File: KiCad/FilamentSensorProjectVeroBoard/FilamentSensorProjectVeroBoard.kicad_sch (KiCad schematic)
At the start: 7 parts, among them J1 Power input, J2 NeoPixels JST-PH, J3 Audio JST-PH, J4 Power JST-PH, J5 Power JST-PH, SW1 Power switch, U1 MCU ESP32-C3 Mini

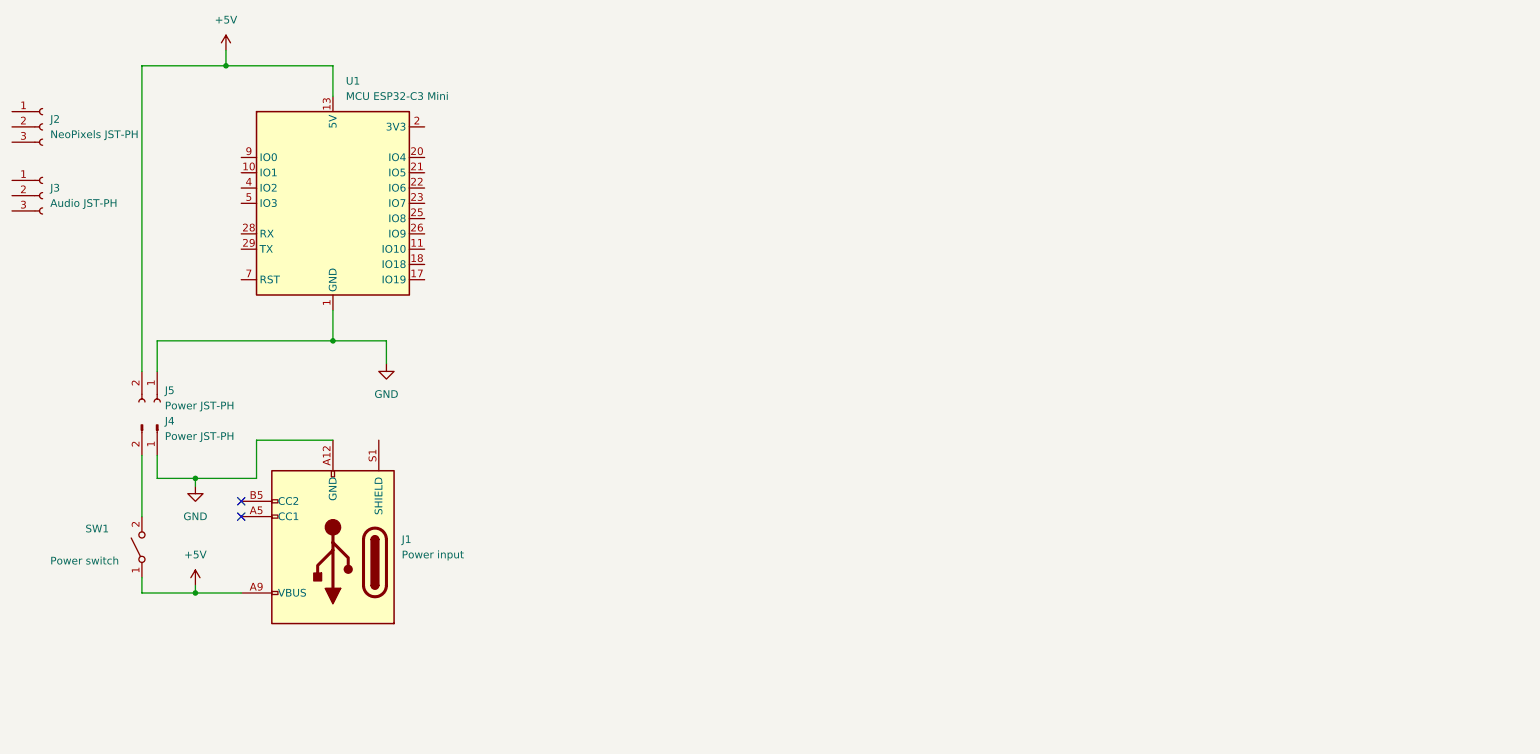
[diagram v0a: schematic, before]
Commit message: Added Vero Board Shematic
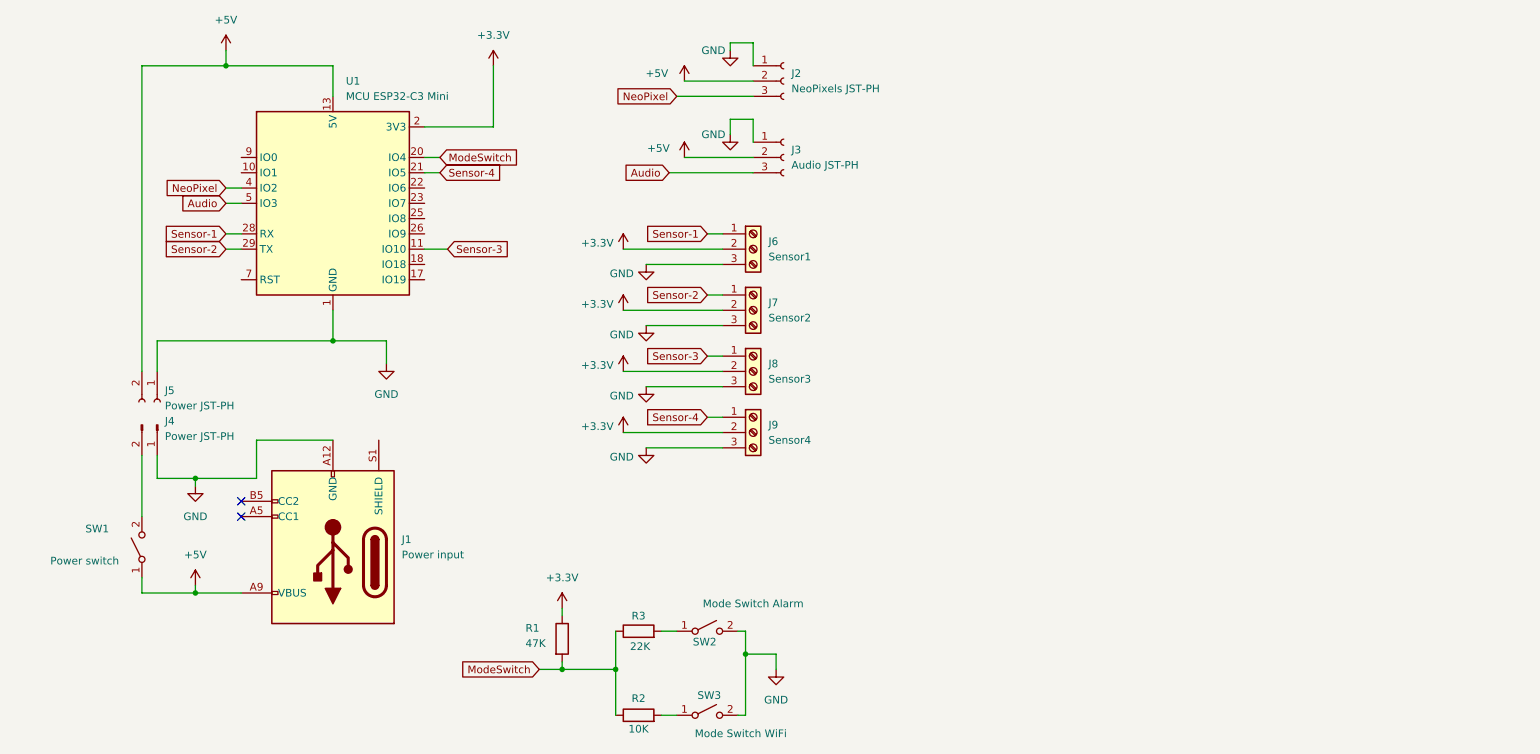
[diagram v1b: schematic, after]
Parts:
- added J6: Sensor1, symbol Connector:Screw_Terminal_01x03
- added J7: Sensor2, symbol Connector:Screw_Terminal_01x03
- added J8: Sensor3, symbol Connector:Screw_Terminal_01x03
- added J9: Sensor4, symbol Connector:Screw_Terminal_01x03
- added R1: 47K, symbol Device:R
- added R2: 10K, symbol Device:R
- added R3: 22K, symbol Device:R
- added SW2: Mode Switch Alarm, symbol Switch:SW_SPST
- added SW3: Mode Switch WiFi, symbol Switch:SW_SPST
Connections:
- net +5V: now also J2.2 (Pin_2), J3.2 (Pin_2)
- net GND: now also J2.1 (Pin_1), J3.1 (Pin_1), J6.3 (Pin_3), J7.3 (Pin_3), J8.3 (Pin_3), J9.3 (Pin_3), SW2.2 (B), SW3.2 (B)
- net Audio: now reaches J3.3 (Pin_3)
- net Audio: now also U1.5 (IO3)
- net NeoPixel: now reaches J2.3 (Pin_3)
- net NeoPixel: now also U1.4 (IO2)
- net Sensor-3: now reaches U1.11 (IO10)
- net Sensor-3: now also J8.1 (Pin_1)
- net +3.3V: now reaches U1.2 (3V3), U1.3 (3V3)
- net +3.3V: now also J6.2 (Pin_2), J7.2 (Pin_2), J8.2 (Pin_2), J9.2 (Pin_2), R1.1
- net ModeSwitch: now reaches U1.20 (IO4)
- net ModeSwitch: now also R1.2, R2.1, R3.1
- net Sensor-4: now reaches U1.21 (IO5)
- net Sensor-4: now also J9.1 (Pin_1)
- net Sensor-1: now reaches U1.28 (RX)
- net Sensor-1: now also J6.1 (Pin_1)
- net Sensor-2: now reaches U1.29 (TX)
- net Sensor-2: now also J7.1 (Pin_1)
- new net: R3.2, SW2.1 (A)
- new net: R2.2, SW3.1 (A)
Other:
- moved on the sheet: J2, J3

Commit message: Added external siren code, updated schematic
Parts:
- added J10: Jack-DC 12v, symbol Connector:Jack-DC
- added J11: 3Pin JST, symbol Connector:Conn_01x03_Pin
- added J12: RCA Jack Alarm 12v, symbol Connector:Conn_Coaxial_Power
- added J13: 3Pin JST, symbol Connector:Conn_01x03_Socket
- added R4: R680, symbol Device:R
- added U2: DC-DC_Mini560 5V, Econode:DC-DC Mini560, symbol Econode2:DC-DC_Mini560
- added U3: PhotoMOS, symbol Isolator:Optocoupler_DC_PhotoNPN_AKEC
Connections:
- net +5V: now also U2.1 (OUT+)
- net GND: now also J10.2, J11.1 (Pin_1), J12.2 (Ext), J13.1 (Pin_1), U2.2 (OUT-), U2.4 (IN-), U3.2
- net AlarmRelay: now reaches U1.23 (IO7)
- net AlarmRelay: now also R4.1
- new net: R4.2, U3.1
- new net: J13.2 (Pin_2), U3.3
- new net: J11.2 (Pin_2), J12.1 (In)
- new net +12V: J10.1, J11.3 (Pin_3), J13.3 (Pin_3), U2.3 (IN+), U3.4
